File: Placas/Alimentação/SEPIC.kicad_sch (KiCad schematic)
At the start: 5 parts, among them J10 Conn_01x01_Pin, J11 Conn_01x01_Pin, J12 Conn_01x01_Pin, J9 Conn_01x01_Pin, U2 Módulo XL6009

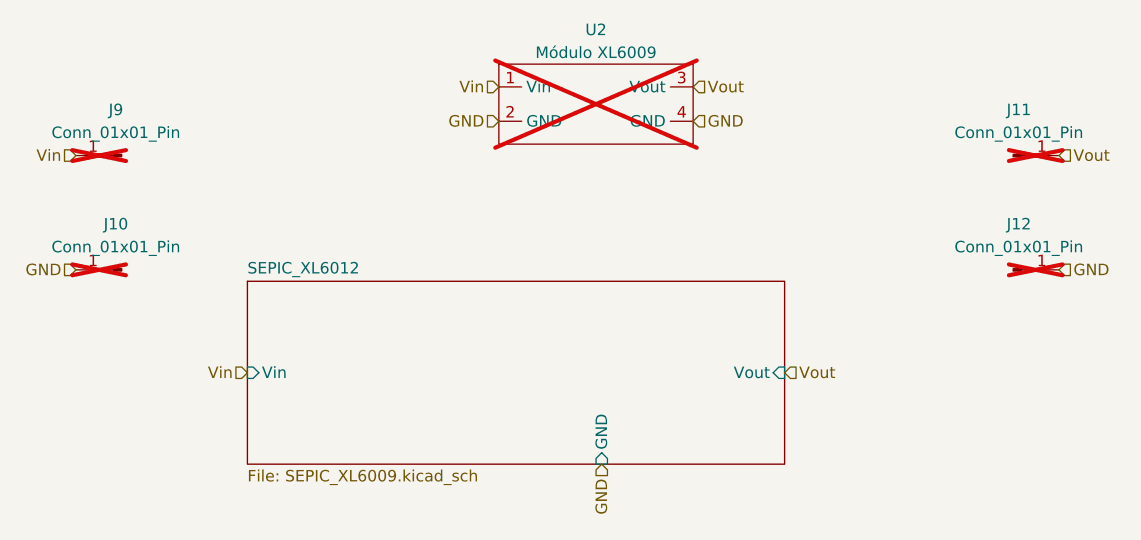
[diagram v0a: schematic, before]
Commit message: Modificações nas duas placas, adição de furos para montagem, melhora na posição dos micros e conectores para comunicação SPI
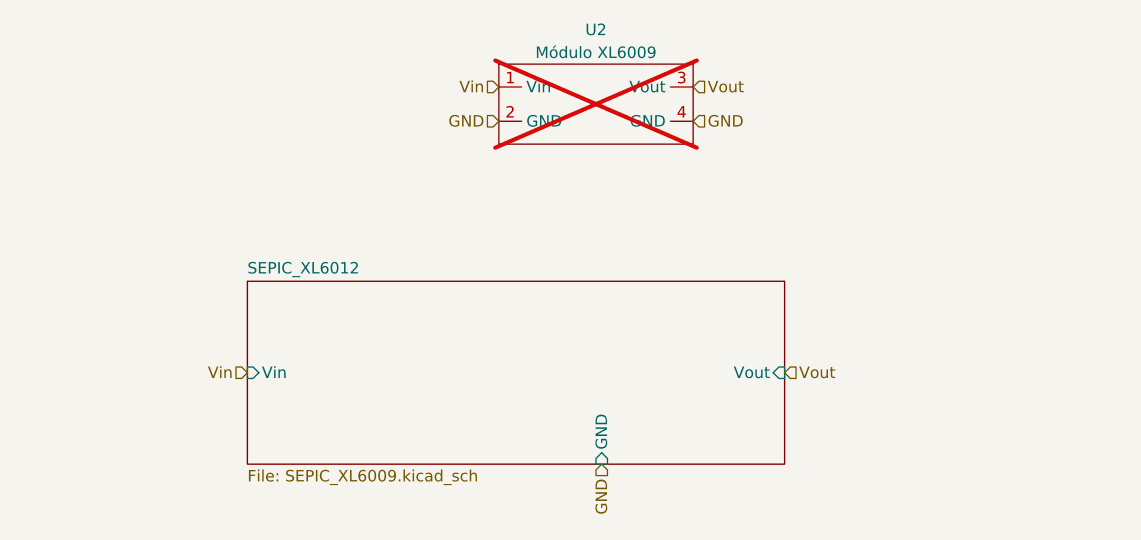
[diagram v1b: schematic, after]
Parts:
- removed J10, J11, J12, J9: Conn_01x01_Pin, Connector_PinHeader_2.54mm:PinHeader_1x01_P2.54mm_Vertical, symbol Connector:Conn_01x01_Pin

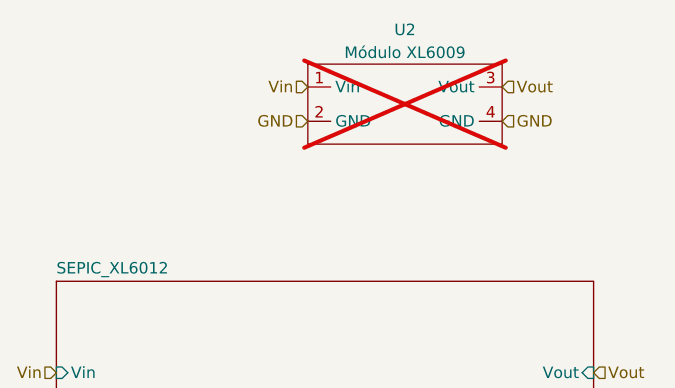
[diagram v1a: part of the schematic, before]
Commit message: Criação dos arquivos em C para o firmware dos dois micros e script em python para salvar aquisição dos dados e envio de comandos
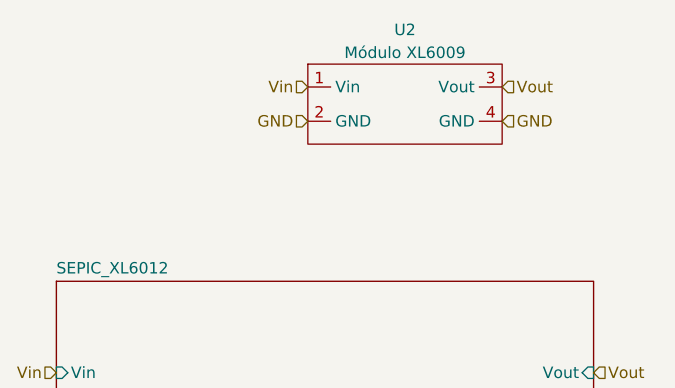
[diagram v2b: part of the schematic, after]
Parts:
- U2: now fitted
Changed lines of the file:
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@@
 		(in_bom yes)
 		(on_board yes)
-		(dnp yes)
+		(dnp no)
 		(fields_autoplaced yes)
 		(property "Reference" "U2"
